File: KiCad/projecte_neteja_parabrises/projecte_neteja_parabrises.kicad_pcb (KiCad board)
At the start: 2 copper layers, 66 parts, among them J1 Conn_01x05_Pin, J2 DE9_Pins, J3 DE9_Pins, K1 G6K-2, K3 Fujitsu_FTR-LYAA005x, M1 Motor_DC, M2 Motor_DC, M3 Motor_DC, M4 Motor_DC, Q1 MMBT3904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

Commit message: Actualizacion errores
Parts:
- added R15: Heater, Resistor_SMD:R_2512_6332Metric_Pad1.40x3.35mm_HandSolder, F.Cu at (87.1, 86.6)
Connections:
- K3 pad 14: Net-(HEATER1-Pad1) -> Net-(K3-Pad14)
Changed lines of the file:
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@@
 	(net 91 "unconnected-(U9-T2IN-Pad10)")
 	(net 92 "unconnected-(U9-T2OUT-Pad7)")
+	(net 93 "Net-(K3-Pad14)")
 	(footprint "Crystal:Crystal_SMD_HC49-SD"
 		(layer "F.Cu")
@@
 		)
 	)
+	(footprint "Resistor_SMD:R_2512_6332Metric_Pad1.40x3.35mm_HandSolder"
+		(layer "F.Cu")
+		(at 87.075 86.625)
+		(descr "Resistor SMD 2512 (6332 Metric), square (rectangular) end terminal, IPC-7351 nominal with elongated pad for handsoldering. (Body size source: IPC-SM-782 page 72, https://www.pcb-3d.com/wordpress/wp-content/uploads/ipc-sm-782a_amendment_1_and_2.pdf), generated with kicad-footprint-generator")
+		(tags "resistor handsolder")
+		(property "Reference" "R15"
+			(at 0 -2.63 0)
+			(layer "F.SilkS")
+			(effects
+				(font
+					(size 1 1)
+					(thickness 0.15)
+				)
+			)
+		)
+		(property "Value" "Heater"
+			(at 0 2.63 0)
+			(layer "F.Fab")
+			(effects
+				(font
+					(size 1 1)
+					(thickness 0.15)
+				)
+			)
+		)
+		(property "Datasheet" "~"
+			(at 0 0 0)
+			(layer "F.Fab")
+			(hide yes)
+			(effects
+				(font
+					(size 1.27 1.27)
+					(thickness 0.15)
+				)
+			)
+		)
+		(property "Description" "Resistive heater"
+			(at 0 0 0)
+			(layer "F.Fab")
+			(hide yes)
+			(effects
+				(font
+					(size 1.27 1.27)
+					(thickness 0.15)
+				)
+			)
+		)
+		(sheetname "/Potencia/")
+		(sheetfile "Potencia.kicad_sch")
+		(attr smd)
+		(fp_line
+			(start -2.177064 -1.71)
+			(end 2.177064 -1.71)
+			(stroke
+				(width 0.12)
+				(type solid)
+			)
+			(layer "F.SilkS")
+		)
+		(fp_line
+			(start -2.177064 1.71)
+			(end 2.177064 1.71)
+			(stroke
+				(width 0.12)
+				(type solid)
+			)
+			(layer "F.SilkS")
+		)
+		(fp_rect
+			(start -4 -1.93)
+			(end 4 1.93)
+			(stroke
+				(width 0.05)
+				(type solid)
+			)
+			(fill no)
+			(layer "F.CrtYd")
+		)
+		(fp_rect
+			(start -3.15 -1.6)
+			(end 3.15 1.6)
+			(stroke
+				(width 0.1)
+				(type solid)
+			)
+			(fill no)
+			(layer "F.Fab")
+		)
+		(fp_text user "${REFERENCE}"
+			(at 0 0 0)
+			(layer "F.Fab")
+			(effects
+				(font
+					(size 1 1)
+					(thickness 0.15)
+				)
+			)
+		)
+		(pad "1" smd roundrect
+			(at -3.05 0)
+			(size 1.4 3.35)
+			(layers "F.Cu" "F.Mask" "F.Paste")
+			(roundrect_rratio 0.178571)
+			(net 93 "Net-(K3-Pad14)")
+			(pintype "passive")
+		)
+		(pad "2" smd roundrect
+			(at 3.05 0)
+			(size 1.4 3.35)
+			(layers "F.Cu" "F.Mask" "F.Paste")
+			(roundrect_rratio 0.178571)
+			(net 2 "GND")
+			(pintype "passive")
+		)
+		(embedded_fonts no)
+		(model "${KICAD9_3DMODEL_DIR}/Resistor_SMD.3dshapes/R_2512_6332Metric.step"
+			(offset
+				(xyz 0 0 0)
+			)
+			(scale
+				(xyz 1 1 1)
+			)
+			(rotate
+				(xyz 0 0 0)
+			)
+		)
+	)
 	(footprint "Capacitor_SMD:C_0805_2012Metric"
 		(layer "F.Cu")
@@
 			(layers "*.Cu" "*.Mask")
 			(remove_unused_layers no)
-			(net 29 "Net-(HEATER1-Pad1)")
+			(net 93 "Net-(K3-Pad14)")
 			(pintype "passive")
 		)

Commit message: actualizacion componentes placa
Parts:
- removed C18: 60, Capacitor_SMD:C_0805_2012Metric
- removed D1: D, Diode_SMD:D_0201_0603Metric_Pad0.64x0.40mm_HandSolder
- removed HEATER1: 1K, Resistor_SMD:R_0603_1608Metric_Pad0.98x0.95mm_HandSolder
- removed K1: G6K-2, Relay_THT:Relay_DPDT_Omron_G6K-2P
- removed M4: Motor_DC, TerminalBlock:TerminalBlock_MaiXu_MX126-5.0-02P_1x02_P5.00mm
- removed Q1: MMBT3904, Package_TO_SOT_SMD:SOT-23
- removed R1: 4.7K, Resistor_SMD:R_0603_1608Metric_Pad0.98x0.95mm_HandSolder
- removed SW3: SW_SP5T_NR01105, Button_Switch_THT:SW_NKK_NR01
- removed U4: DRV8871DDA, Package_SO:Texas_HTSOP-8-1EP_3.9x4.9mm_P1.27mm_EP2.95x4.9mm_Mask2.4x3.1mm_ThermalVias
- added C10: 47u, Capacitor_SMD:C_0805_2012Metric_Pad1.18x1.45mm_HandSolder, F.Cu at (78.9, 98.9)
- added C16: 100n, Capacitor_SMD:C_0805_2012Metric, F.Cu at (78.7, 88.3)
- added D5: D, Diode_SMD:D_0201_0603Metric_Pad0.64x0.40mm_HandSolder, F.Cu at (118.3, 90.0)
- added D6: D, Diode_SMD:D_0201_0603Metric_Pad0.64x0.40mm_HandSolder, F.Cu at (118.3, 91.7)
- added FB1: FerriteBead, Ferrite_THT:LairdTech_28C0236-0JW-10, F.Cu at (109.6, 91.8)
- added K2: Fujitsu_FTR-LYAA005x, Relay_THT:Relay_SPST-NO_Fujitsu_FTR-LYAA005x_FormA_Vertical, F.Cu at (122.1, 80.3)
- added K4: Fujitsu_FTR-LYAA005x, Relay_THT:Relay_SPST-NO_Fujitsu_FTR-LYAA005x_FormA_Vertical, F.Cu at (122.1, 93.8)
- added M5: Motor_DC, TerminalBlock:TerminalBlock_MaiXu_MX126-5.0-02P_1x02_P5.00mm, F.Cu at (111.7, 77.4)
- added Q2: MMBT3904, Package_TO_SOT_SMD:SOT-23, F.Cu at (146.1, 44.2)
- added Q4: MMBT3904, Package_TO_SOT_SMD:SOT-23, F.Cu at (146.1, 53.1)
- added R16: 10K, Resistor_SMD:R_0603_1608Metric_Pad0.98x0.95mm_HandSolder, F.Cu at (80.8, 114.3)
- added R17: 60, Resistor_SMD:R_0201_0603Metric_Pad0.64x0.40mm_HandSolder, F.Cu at (80.0, 104.4)
- added R18: 7.6k, Resistor_SMD:R_0603_1608Metric_Pad0.98x0.95mm_HandSolder, F.Cu at (141.5, 55.8)
- added R19: 10K, Resistor_SMD:R_0201_0603Metric_Pad0.64x0.40mm_HandSolder, F.Cu at (80.0, 106.2)
- added R20: 10K, Resistor_SMD:R_0201_0603Metric_Pad0.64x0.40mm_HandSolder, F.Cu at (80.0, 107.9)
- added R21: 10K, Resistor_SMD:R_0201_0603Metric_Pad0.64x0.40mm_HandSolder, F.Cu at (80.0, 109.7)
- added R22: 7.6k, Resistor_SMD:R_0603_1608Metric_Pad0.98x0.95mm_HandSolder, F.Cu at (141.5, 58.3)
- added R23: 7.6k, Resistor_SMD:R_0603_1608Metric_Pad0.98x0.95mm_HandSolder, F.Cu at (141.5, 60.8)
- added SW5: SW_SP3T_NR01103, Button_Switch_THT:SW_NKK_NR01, F.Cu at (167.2, 88.5)
- C19: value 60 -> 100p
- R11: value 4,7k -> Heater; footprint Resistor_SMD:R_0603_1608Metric_Pad0.98x0.95mm_HandSolder -> Resistor_SMD:R_2512_6332Metric_Pad1.40x3.35mm_HandSolder
- R12: value 4,7k -> 60; footprint Resistor_SMD:R_0603_1608Metric_Pad0.98x0.95mm_HandSolder -> Resistor_SMD:R_0201_0603Metric_Pad0.64x0.40mm_HandSolder
- R13, R14: value 470 -> 4.7K
- R15: value Heater -> 10K; footprint Resistor_SMD:R_2512_6332Metric_Pad1.40x3.35mm_HandSolder -> Resistor_SMD:R_0603_1608Metric_Pad0.98x0.95mm_HandSolder
- R7, R8: value R -> 1k
- U7: value SN74LVC2T45DCUR -> DRV8871DDA; footprint Package_SO:VSSOP-8_2.3x2mm_P0.5mm -> Package_SO:Texas_HTSOP-8-1EP_3.9x4.9mm_P1.27mm_EP2.95x4.9mm_Mask2.4x3.1mm_ThermalVias
- moved U8 103.8 mm to (79.5, 95.1)
- moved C19 103.8 mm to (78.7, 91.3)
- moved C5 103.8 mm to (78.7, 73.2)
- moved C6 103.8 mm to (78.7, 76.3)
- moved C7 103.8 mm to (78.7, 79.3)
- moved C8 103.8 mm to (78.7, 82.3)
- moved C9 103.8 mm to (78.7, 85.3)
- moved J3 78.2 mm to (215.1, 108.8), turned to 90 degrees
- moved R13 67.5 mm to (141.5, 50.8)
- moved R14 67.5 mm to (141.5, 53.3)
- moved R8 66.7 mm to (158.7, 126.7)
- moved J2 66.4 mm to (214.7, 71.0), turned to 90 degrees
- moved U5 66.1 mm to (170.4, 71.6)
- moved K3 49.9 mm to (122.1, 87.0)
- moved U7 47.4 mm to (144.0, 72.1)
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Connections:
- C19 pad 1: Net-(U8-CANH) -> Net-(C19-Pad1)
- D2 pad 2: VCC -> VDD
- J1 pad 2: VCC -> VDD
- M3 pad 2: GND -> GND_PWR
- R10 pad 1: GND -> SDA
- R10 pad 2: Net-(U6-SDA) -> VDD
- R11 pad 1: GND -> Net-(K3-Pad14)
- R11 pad 2: SDA -> unconnected-(R11-Pad2)
- R12 pad 1: SCL -> Net-(U8-CANH)
- R12 pad 2: GND -> Net-(C19-Pad1)
- R13 pad 1: Net-(U5-RB7) -> GATE B
- R13 pad 2: PGD -> Net-(Q2-B)
- R14 pad 1: Net-(U5-RB6) -> GATE B
- R14 pad 2: PGC -> Net-(Q4-B)
- R15 pad 1: Net-(K3-Pad14) -> VDD
- R15 pad 2: GND -> SWB
- R2 pad 1: GND -> VCC
- R3 pad 1: FC2 -> VCC
- R3 pad 2: GND -> FC2
- R9 pad 1: Net-(U6-SCL) -> VDD
- R9 pad 2: GND -> SCL
- U3 pad 1: GND -> GND_PWR
- U3 pad 3: PGC -> PWM2
- U3 pad 7: GND -> GND_PWR
- U3 pad 9: GND -> GND_PWR
- U5 pad 12: SW4 -> FC1
- U5 pad 14: SW5 -> FC2
- U5 pad 15: Net-(U5-RB6) -> PGC
- U5 pad 16: Net-(U5-RB7) -> PGD
- U5 pad 21: FC1 -> PWM
- U5 pad 24: FC2 -> PWM2
- U6 pad 1: Net-(U6-SDA) -> SDA
- U6 pad 5: Net-(U6-VDD) -> VDD
- U6 pad 6: Net-(U6-SCL) -> SCL
- U7 pad 1: Net-(U6-VDD) -> GND_PWR
- U7 pad 2: Net-(U6-SDA) -> GND
- U7 pad 3: Net-(U6-SCL) -> PWM
- U7 pad 4: GND -> unconnected-(U7-ILIM-Pad4)
- U7 pad 5: GND -> 12V
- U7 pad 6: SCL -> Net-(M1-+)
- U7 pad 7: SDA -> GND_PWR
- U7 pad 8: VDD -> Net-(M1--)

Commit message: micro
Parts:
- moved C10 94.2 mm to (171.4, 80.8)
- moved R15 94.2 mm to (173.2, 93.7)
- moved R16 94.2 mm to (173.2, 96.3)
- moved U8 94.2 mm to (172.0, 77.0)
- moved C16 94.2 mm to (171.2, 70.2)
- moved C19 94.2 mm to (171.2, 73.2)
- moved C5 94.2 mm to (171.2, 55.2)
- moved C6 94.2 mm to (171.2, 58.2)
- moved C7 94.2 mm to (171.2, 61.2)
- moved C8 94.2 mm to (171.2, 64.2)
- moved C9 94.2 mm to (171.2, 67.2)
- moved R12 94.2 mm to (172.5, 84.6)
- moved R17 94.2 mm to (172.5, 86.4)
- moved R19 94.2 mm to (172.5, 88.1)
- moved R20 94.2 mm to (172.5, 89.9)
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
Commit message: huella
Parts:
- added U4: PIC24HJ64GP504, Package_DFN_QFN:QFN-44-1EP_7x7mm_P0.5mm_EP5.2x5.2mm, F.Cu at (129.9, 116.0)
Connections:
- C1 pad 1: Net-(U5-AVDD) -> Net-(U4-AVdd)
- C17 pad 1: Net-(U5-VCAP) -> Net-(U4-VCAP)
- R13 pad 1: GATE B -> GATE B2

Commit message: pcb
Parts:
- removed U5: PIC24HJ32GP502, Package_SO:SOIC-28W_7.5x17.9mm_P1.27mm
- moved L1 116.4 mm to (46.0, 147.8)
- moved R5 116.4 mm to (46.0, 150.3)
- moved R6 116.4 mm to (46.0, 152.9)
- moved R8 116.4 mm to (46.0, 155.4)
- moved R13 109.8 mm to (227.2, 103.4)
- moved R14 109.8 mm to (227.2, 105.9)
- moved R18 109.8 mm to (227.2, 108.4)
- moved R2 109.8 mm to (227.2, 95.9)
- moved R22 109.8 mm to (227.2, 110.9)
- moved R23 109.8 mm to (227.2, 113.4)
- moved R3 109.8 mm to (227.2, 98.4)
- moved R4 109.8 mm to (227.2, 100.9)
- moved R16 98.5 mm to (261.5, 52.7), turned to 90 degrees
- moved R15 95.1 mm to (259.0, 52.7), turned to 90 degrees
- moved R21 92.7 mm to (256.9, 53.4), turned to 90 degrees
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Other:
- board outline added: 100 x 99.9 mm

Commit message: placements restantes
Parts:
- moved R9 145.2 mm to (146.7, 88.5), turned to -90 degrees
- moved R10 141.8 mm to (141.0, 88.6), turned to 90 degrees
- moved R4 138.3 mm to (92.9, 133.6), turned to 90 degrees
- moved R18 137.1 mm to (92.0, 131.2), turned to 180 degrees
- moved R2 136.7 mm to (94.0, 65.2)
- moved R13 136.5 mm to (92.2, 123.1)
- moved R22 134.8 mm to (93.2, 125.7), turned to -90 degrees
- moved R6 134.1 mm to (177.2, 125.5), turned to 90 degrees
- moved R5 131.7 mm to (175.3, 125.5), turned to -90 degrees
- moved R15 130.8 mm to (128.8, 65.4), turned to 180 degrees
- moved R8 129.2 mm to (171.0, 123.0), turned to -90 degrees
- moved R14 127.0 mm to (101.4, 123.0)
- moved R7 126.7 mm to (117.8, 78.9)
- moved R23 125.5 mm to (102.3, 125.5), turned to -90 degrees
- moved R16 123.8 mm to (138.4, 65.4), turned to 180 degrees
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
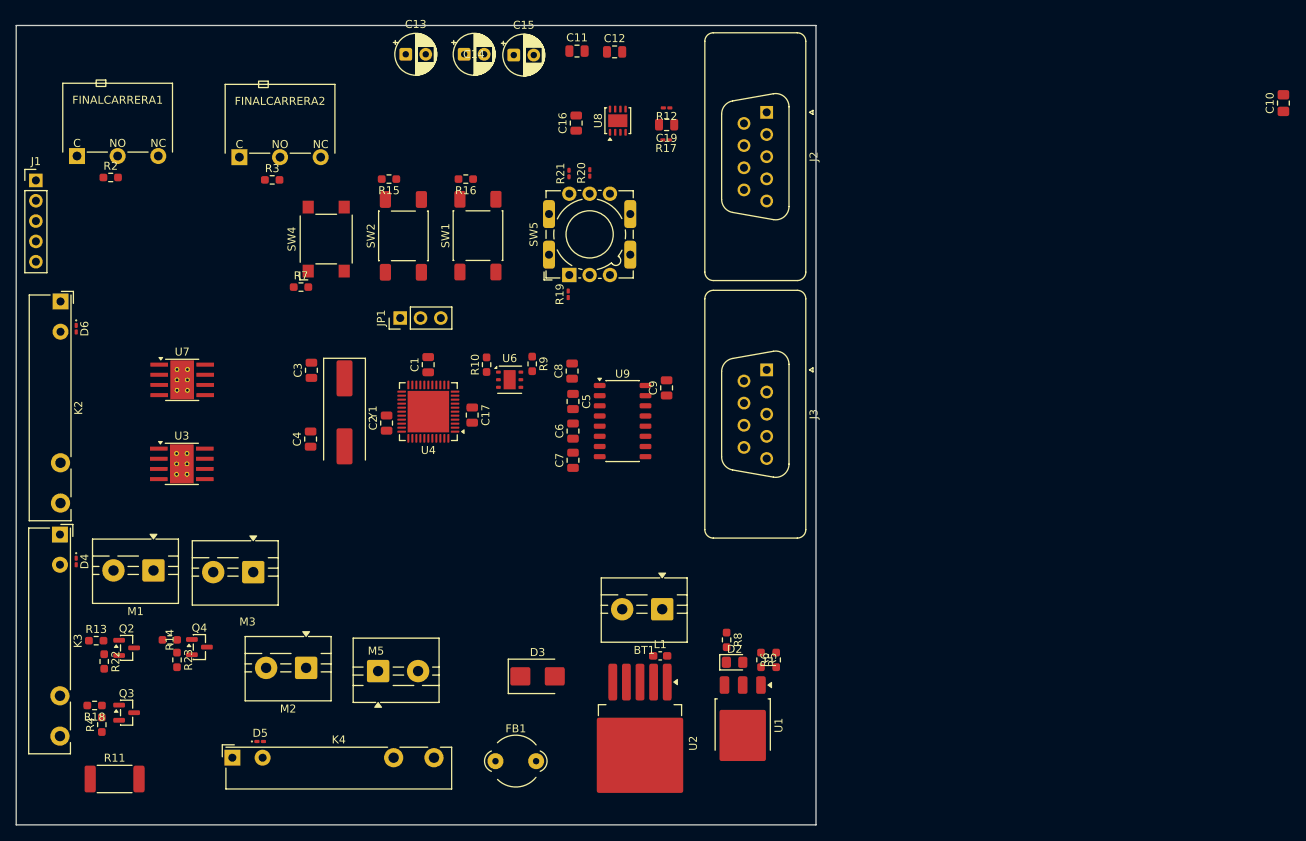
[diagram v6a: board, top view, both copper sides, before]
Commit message: pcb placement
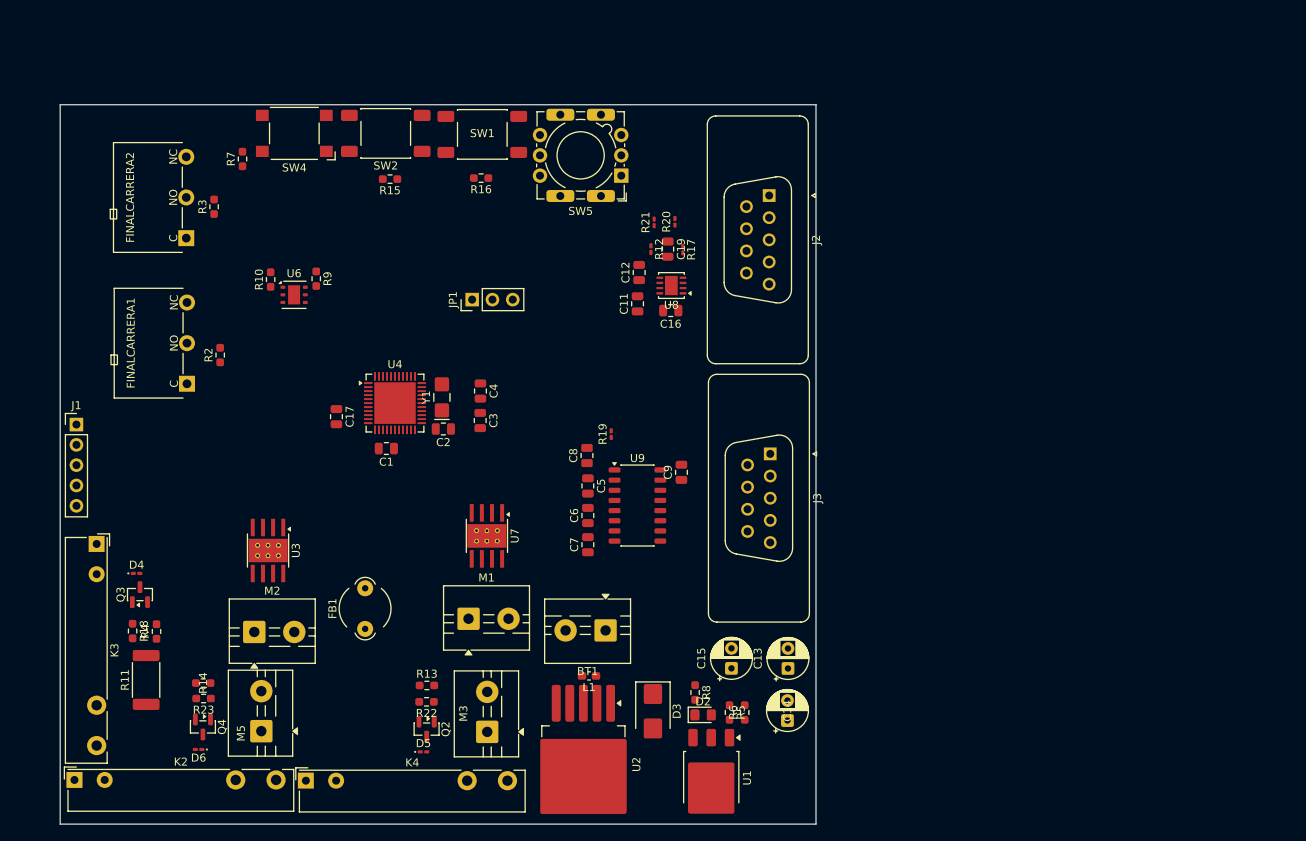
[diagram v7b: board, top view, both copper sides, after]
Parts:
- removed C10: 47u, Capacitor_SMD:C_0805_2012Metric_Pad1.18x1.45mm_HandSolder
- Y1: footprint Crystal:Crystal_SMD_HC49-SD -> Crystal:Crystal_SMD_EuroQuartz_EQ161-2Pin_3.2x1.5mm_HandSoldering
- moved C14 92.6 mm to (178.6, 133.1), turned to 90 degrees
- moved C13 90.4 mm to (178.7, 126.6), turned to 90 degrees
- moved C15 81.3 mm to (171.6, 126.6), turned to 90 degrees
- moved K2 59.8 mm to (89.5, 140.5), turned to 0 degrees
- moved D6 54.8 mm to (105.0, 136.7), turned to 180 degrees
- moved U7 42.8 mm to (141.0, 110.0), turned to -90 degrees
- moved R13 41.7 mm to (133.5, 128.7)
- moved R22 40.6 mm to (133.5, 130.7), turned to 180 degrees
- moved M1 39.8 mm to (138.7, 120.4), turned to 0 degrees
- moved Q2 38.9 mm to (133.5, 134.2), turned to -90 degrees
- moved M3 35.4 mm to (141.1, 134.5), turned to 90 degrees
- moved C11 32.5 mm to (159.9, 81.0), turned to 90 degrees
- moved FINALCARRERA1 31.6 mm to (103.5, 91.0), turned to 90 degrees
- moved J1 30.9 mm to (89.7, 96.1)
- moved R10 29.0 mm to (114.0, 78.0)
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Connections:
- R11 pad 2: unconnected-(R11-Pad2) -> GND_PWR
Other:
- board size 100 x 99.9 mm -> 94.5 x 89.9 mm

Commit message: pcb
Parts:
- removed SW4: SW_Omron_B3FS, Button_Switch_SMD:SW_SPST_Omron_B3FS-100xP
- added J4: Conn_01x02_Pin, Connector_PinHeader_2.54mm:PinHeader_1x02_P2.54mm_Vertical, F.Cu at (102.5, 100.0)
- added SW3: CALEFACTOR, Button_Switch_SMD:SW_Push_SPST_NO_Alps_SKRK, F.Cu at (119.8, 59.8)
- J2, J3: footprint Connector_Dsub:DSUB-9_Pins_Vertical_P2.77x2.84mm -> Connector_Dsub:DSUB-9_Pins_Horizontal_P2.77x2.84mm_EdgePinOffset9.40mm
- SW1, SW2: footprint Button_Switch_SMD:SW_Push_1P1T_NO_E-Switch_TL3301NxxxxxG -> Button_Switch_SMD:SW_Push_SPST_NO_Alps_SKRK
- moved C13 29.6 mm to (208.3, 127.9)
- moved C14 29.5 mm to (208.0, 135.3)
- moved SW5 12.3 mm to (146.3, 60.8), turned to 0 degrees
- moved J3 12.1 mm to (180.9, 111.1), turned to 90 degrees
- moved J2 11.8 mm to (180.6, 78.4), turned to 90 degrees
- moved BT1 10.00 mm to (165.8, 120.9)
- moved D2 10.00 mm to (178.0, 131.4)
- moved D3 10.00 mm to (171.7, 131.0)
- moved R6 10.00 mm to (183.2, 131.1)
- moved R8 10.00 mm to (177.0, 128.6)
- moved U2 10.00 mm to (163.0, 137.6)
- moved C15 10.00 mm to (181.6, 125.6)
- moved L1 10.00 mm to (163.7, 126.5)
- moved R5 10.00 mm to (181.3, 131.1)
- moved U1 10.00 mm to (179.0, 139.3)
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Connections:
- C11 pad 1: Net-(BT1-+) -> Vbat
- U2 pad 1: Net-(BT1-+) -> Vbat
- U4 pad 14: unconnected-(U4-RB14-Pad14) -> GATE C
- U4 pad 19: SWC -> GATE B2
- U4 pad 2: SW1 -> unconnected-(U4-RC6-Pad2)
- U4 pad 20: SWB -> GATE B
- U4 pad 25: GATE B -> CANRX
- U4 pad 26: GATE B2 -> CANTX
- U4 pad 27: GATE C -> unconnected-(U4-RC2-Pad27)
- U4 pad 3: SW2 -> FC2
- U4 pad 32: FC1 -> unconnected-(U4-RA8-Pad32)
- U4 pad 33: FC2 -> unconnected-(U4-RB4-Pad33)
- U4 pad 35: unconnected-(U4-RA9-Pad35) -> SW1
- U4 pad 36: CANRX -> SW2
- U4 pad 37: CANTX -> SW3
- U4 pad 4: SW3 -> FC1
- U4 pad 41: unconnected-(U4-RB5-Pad41) -> SWC
- U4 pad 42: unconnected-(U4-RB6-Pad42) -> SWB
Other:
- board size 94.5 x 89.9 mm -> 106.5 x 95.3 mm
